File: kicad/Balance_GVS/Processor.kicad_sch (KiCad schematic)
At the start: 21 parts, among them SW3 SW_Push, SW4 SW_Push, U1 ESP32-WROOM-32E, U10 INA219BxD, U2 ESP32-WROOM-32E-N4, U9 MCP4725xxx-xCH

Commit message: Add 3.3V Voltage Regulator and ESP32 Battery ADC
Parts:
- added R33, R34: 10K, symbol Device:R
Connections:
- net GND: now also R34.2
- net Battery_ADC: now reaches U1.8 (IO32)
- net Battery_ADC: now also R33.2, R34.1
- new net Battery_Voltage: R33.1

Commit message: Started adding howland connections
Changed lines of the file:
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@@
 	)
 	(global_label "DAC_OUT"
-		(shape input)
+		(shape output)
 		(at 153.67 63.5 0)
 		(fields_autoplaced yes)

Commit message: Finish Howland
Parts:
- added C22, C23: 4.7µF, symbol Device:C
- added U6: (no value), Package_TO_SOT_SMD:SOT-89-5_Handsoldering, symbol GVS_Library:R1172H331B-T1-FE
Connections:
- net +3.3V: now also C23.2, U6.5 (VOUT)
- net Battery_Voltage: now also C22.1, U6.1 (CE), U6.4 (VIN)
- net GND: now also C22.2, C23.1, U6.2 (GND)

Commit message: Add Processor User IO
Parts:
- removed U2: ESP32-WROOM-32E-N4, ESP32-WROOM_32E_N4_footprints:ESP32­WROOM­32E_EXP, symbol ESP32-WROOM_32E_N4:ESP32-WROOM-32E-N4
- added C24, C25: 0.1uF, RF_Converter:Balun_Johanson_0900PC15J0013, symbol Device:C
- added D5, D6, D7, D8: LED_Small, symbol Device:LED_Small
- added R43, R44, R49, R50: 10K, symbol Device:R
- added R45, R46, R47, R48: 300, symbol Device:R
- added RV1: R_Potentiometer, Package_SO:TSSOP-20_4.4x6.5mm_P0.65mm, symbol Device:R_Potentiometer
- added SW5, SW6: SW_Push, RF_Module:ESP32-WROOM-32E, symbol Switch:SW_Push
- added SW8: SW_DIP_x02, symbol Switch:SW_DIP_x02
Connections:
- net +3.3V: now also R43.1, R44.1, R49.1, R50.1, RV1.1
- net GND: now also C24.2, C25.2, D5.1 (K), D6.1 (K), D7.1 (K), D8.1 (K), RV1.3, SW5.1, SW6.1, SW8.3, SW8.4
- net Button2: now reaches U1.10 (IO25)
- net Button2: now also C25.1, R44.2, SW6.2
- net Switch1: now reaches U1.11 (IO26)
- net Switch1: now also R49.2, SW8.1
- net Switch2: now reaches U1.12 (IO27)
- net Switch2: now also R50.2, SW8.2
- net LED2: now reaches U1.13 (IO14)
- net LED2: now also R46.2
- net LED1: now reaches U1.16 (IO13)
- net LED1: now also R45.2
- net LED3: now reaches U1.23 (IO15)
- net LED3: now also R47.2
- net LED4: now reaches U1.27 (IO16)
- net LED4: now also R48.2
- net Button1: now reaches U1.37 (IO23)
- net Button1: now also C24.1, R43.2, SW5.2
- net POT_ADC: now reaches U1.9 (IO33)
- net POT_ADC: now also RV1.2
- new net: D8.2 (A), R48.1
- new net: D5.2 (A), R45.1
- new net: D7.2 (A), R47.1
- new net: D6.2 (A), R46.1
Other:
- moved on the sheet: C11, C12, C13, C14, C15, C16, C22, C23, R1, R21, R22, R23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

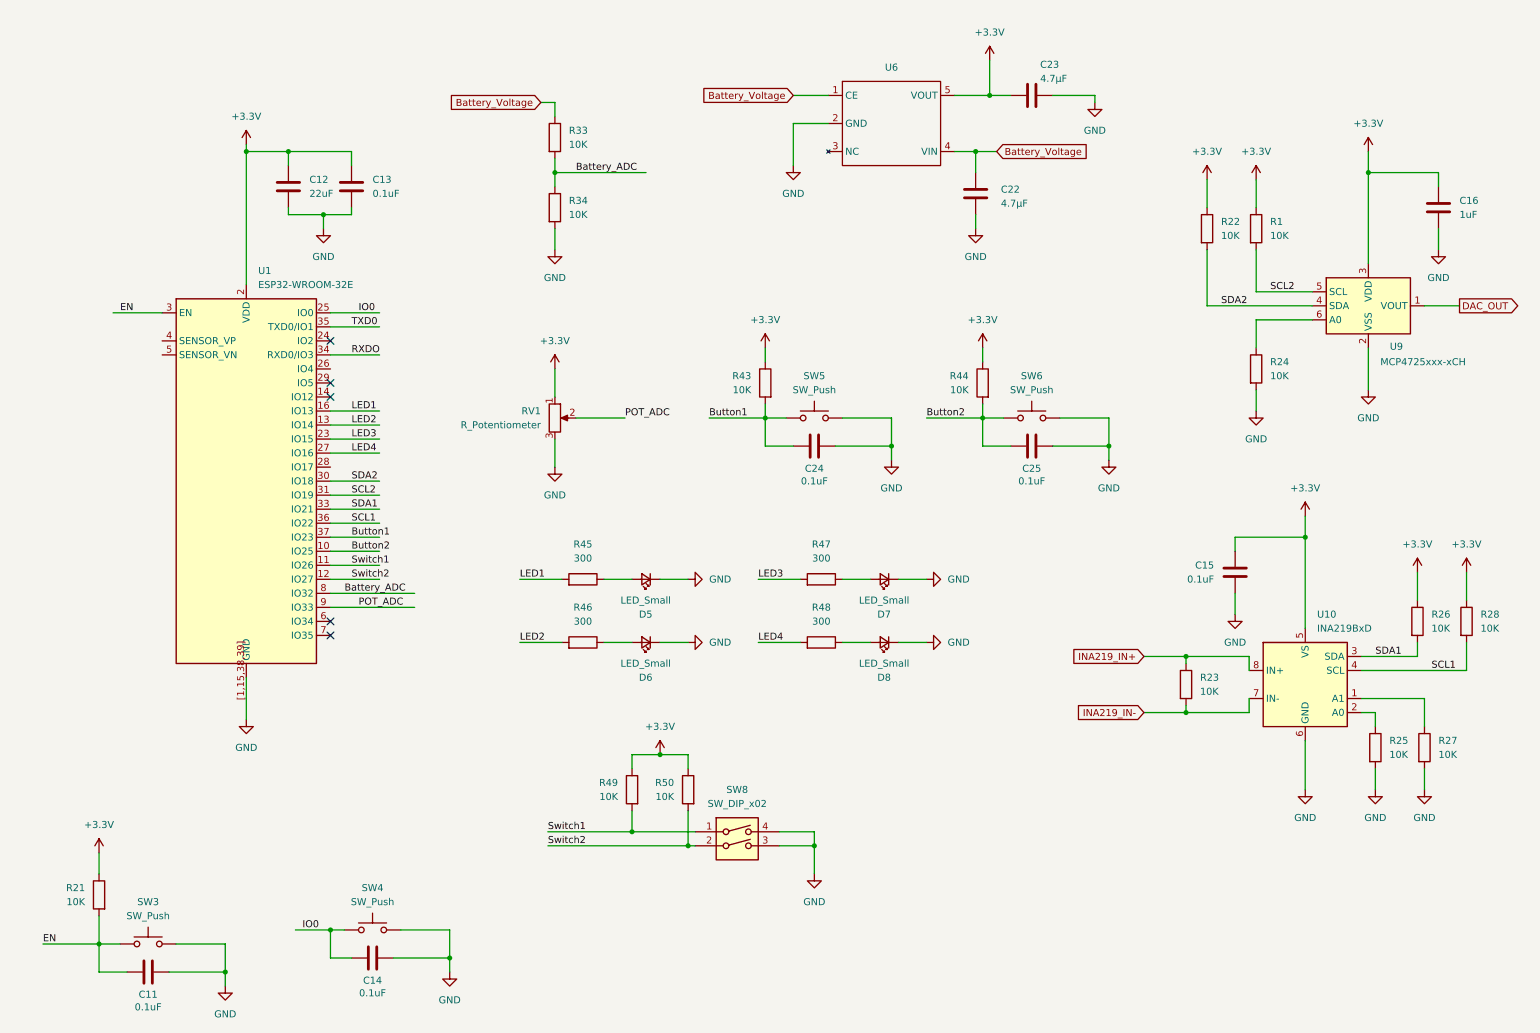
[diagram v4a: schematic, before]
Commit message: Add Footprints to Schematic
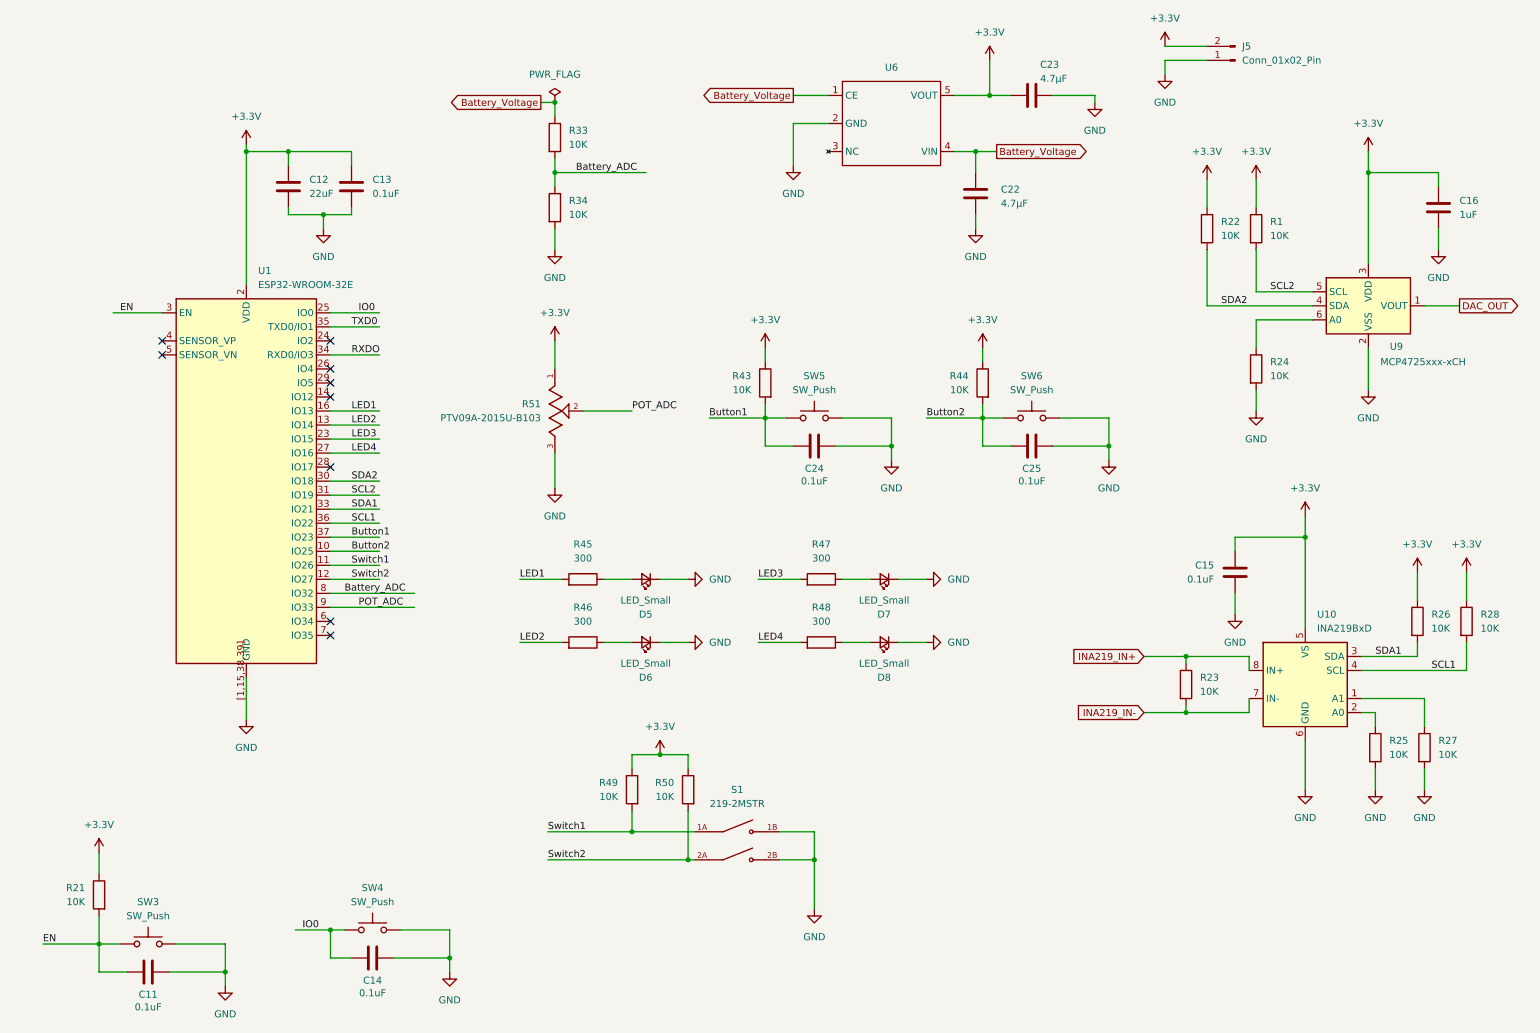
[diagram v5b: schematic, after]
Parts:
- removed RV1: R_Potentiometer, Package_SO:TSSOP-20_4.4x6.5mm_P0.65mm, symbol Device:R_Potentiometer
- removed SW8: SW_DIP_x02, symbol Switch:SW_DIP_x02
- added J5: Conn_01x02_Pin, Connector_PinSocket_2.54mm:PinSocket_1x02_P2.54mm_Vertical, symbol Connector:Conn_01x02_Pin
- added R51: PTV09A-2015U-B103, PTV09A_2015U_B103:TRIM_PTV09A-2015U-B103, symbol PTV09A_2015U_B103:PTV09A-2015U-B103
- added S1: 219-2MSTR, 219_2MSTR:SW_219-2MSTR, symbol 219_2MSTR:219-2MSTR
- C11, C14, C24, C25: footprint RF_Converter:Balun_Johanson_0900PC15J0013 -> Capacitor_SMD:C_0805_2012Metric_Pad1.18x1.45mm_HandSolder
- C12, C13, C15, C16, C22, C23: footprint (none) -> Capacitor_SMD:C_0805_2012Metric_Pad1.18x1.45mm_HandSolder
- D5, D6, D7, D8: footprint (none) -> LED_SMD:LED_0603_1608Metric_Pad1.05x0.95mm_HandSolder
- R1, R21, R22, R23, R24, R25, R26, R27, R28, R33, R34, R43, R44, R45, R46, R47, R48, R49, R50: footprint (none) -> Resistor_SMD:R_0805_2012Metric_Pad1.20x1.40mm_HandSolder
- SW3, SW4, SW5, SW6: footprint RF_Module:ESP32-WROOM-32E -> FSMSMTR:SWITCH_FSMSMTR_TYC
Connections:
- net +3.3V: now also J5.2 (Pin_2), R51.1
- net GND: now also J5.1 (Pin_1), R51.3, S1.1B, S1.2B
- net POT_ADC: now also R51.2
- net Switch1: now also S1.1A
- net Switch2: now also S1.2A
- no-connect marks 5 -> 9

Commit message: Add shit ton to schematic
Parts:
- added J10: I2C Header 2, Connector_PinSocket_2.54mm:PinSocket_1x02_P2.54mm_Vertical, symbol Connector:Conn_01x02_Pin
- added J9: I2C Header 1, Connector_PinSocket_2.54mm:PinSocket_1x02_P2.54mm_Vertical, symbol Connector:Conn_01x02_Pin
- R23: value 10K -> 33
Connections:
- net SCL1: now also J10.2 (Pin_2)
- net SCL2: now also J9.2 (Pin_2)
- net SDA1: now also J10.1 (Pin_1)
- net SDA2: now also J9.1 (Pin_1)
- net INA219_IN+ renamed Safety-
- net INA219_IN- renamed Current_Sense-
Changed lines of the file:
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@@
 	(wire
 		(pts
-			(xy 68.58 106.68) (xy 77.47 106.68)
+			(xy 68.58 106.68) (xy 81.28 106.68)
 		)
 		(stroke
@@
 	(wire
 		(pts
-			(xy 68.58 104.14) (xy 77.47 104.14)
+			(xy 68.58 104.14) (xy 81.28 104.14)
 		)
 		(stroke
@@
 	(wire
 		(pts
-			(xy 68.58 99.06) (xy 77.47 99.06)
+			(xy 68.58 99.06) (xy 81.28 99.06)
 		)
 		(stroke
@@
 	(wire
 		(pts
-			(xy 68.58 101.6) (xy 77.47 101.6)
+			(xy 68.58 101.6) (xy 81.28 101.6)
 		)
 		(stroke
@@
 		)
 	)
-	(global_label "Battery_Voltage"
-		(shape output)
-		(at 152.4 29.21 180)
+	(global_label "Current_Sense-"
+		(shape bidirectional)
+		(at 215.9 140.97 180)
 		(fields_autoplaced yes)
 		(effects
@@
 		)
 		(property "Intersheetrefs" "${INTERSHEET_REFS}"
-			(at 134.7193 29.21 0)
+			(at 196.745 140.97 0)
 			(hide yes)
 			(show_name no)
@@
 		)
 	)
-	(global_label "DAC_OUT"
+	(global_label "Battery_Voltage"
 		(shape output)
-		(at 273.05 67.31 0)
+		(at 152.4 29.21 180)
 		(fields_autoplaced yes)
 		(effects
@@
 				(size 1.27 1.27)
 			)
-			(justify left)
+			(justify right)
 		)
 		(property "Intersheetrefs" "${INTERSHEET_REFS}"
-			(at 284.26 67.31 0)
+			(at 134.7193 29.21 0)
 			(hide yes)
 			(show_name no)
@@
 					(size 1.27 1.27)
 				)
-				(justify left)
+				(justify right)
 			)
 		)
 	)
-	(global_label "Battery_Voltage"
+	(global_label "DAC_OUT"
 		(shape output)
-		(at 106.68 30.48 180)
+		(at 273.05 67.31 0)
 		(fields_autoplaced yes)
 		(effects
@@
 				(size 1.27 1.27)
 			)
-			(justify right)
+			(justify left)
 		)
 		(property "Intersheetrefs" "${INTERSHEET_REFS}"
-			(at 88.9993 30.48 0)
+			(at 284.26 67.31 0)
 			(hide yes)
 			(show_name no)
@@
 					(size 1.27 1.27)
 				)
-				(justify right)
+				(justify left)
 			)
 		)
 	)
-	(global_label "INA219_IN-"
-		(shape input)
-		(at 215.9 140.97 180)
+	(global_label "Battery_Voltage"
+		(shape output)
+		(at 106.68 30.48 180)
 		(fields_autoplaced yes)
 		(effects
@@
 		)
 		(property "Intersheetrefs" "${INTERSHEET_REFS}"
-			(at 201.7871 140.97 0)
+			(at 88.9993 30.48 0)
 			(hide yes)
 			(show_name no)
@@
 		)
 	)
-	(global_label "INA219_IN+"
-		(shape input)
+	(global_label "Safety-"
+		(shape bidirectional)
 		(at 215.9 130.81 180)
 		(fields_autoplaced yes)
@@
 		)
 		(property "Intersheetrefs" "${INTERSHEET_REFS}"
-			(at 201.7871 130.81 0)
+			(at 204.365 130.81 0)
 			(hide yes)
 			(show_name no)
@@
 	)
 	(symbol
+		(lib_id "Connector:Conn_01x02_Pin")
+		(at 86.36 104.14 0)
+		(mirror y)
+		(unit 1)
+		(body_style 1)
+		(exclude_from_sim no)
+		(in_bom yes)
+		(on_board yes)
+		(in_pos_files yes)
+		(dnp no)
+		(property "Reference" "J10"
+			(at 87.63 106.6801 0)
+			(show_name no)
+			(do_not_autoplace no)
+			(effects
+				(font
+					(size 1.27 1.27)
+				)
+				(justify right)
+			)
+		)
+		(property "Value" "I2C Header 2"
+			(at 87.63 104.1401 0)
+			(show_name no)
+			(do_not_autoplace no)
+			(effects
+				(font
+					(size 1.27 1.27)
+				)
+				(justify right)
+			)
+		)
+		(property "Footprint" "Connector_PinSocket_2.54mm:PinSocket_1x02_P2.54mm_Vertical"
+			(at 86.36 104.14 0)
+			(hide yes)
+			(show_name no)
+			(do_not_autoplace no)
+			(effects
+				(font
+					(size 1.27 1.27)
+				)
+			)
+		)
+		(property "Datasheet" ""
+			(at 86.36 104.14 0)
+			(hide yes)
+			(show_name no)
+			(do_not_autoplace no)
+			(effects
+				(font
+					(size 1.27 1.27)
+				)
+			)
+		)
+		(property "Description" "Generic connector, single row, 01x02, script generated"
+			(at 86.36 104.14 0)
+			(hide yes)
+			(show_name no)
+			(do_not_autoplace no)
+			(effects
+				(font
+					(size 1.27 1.27)
+				)
+			)
+		)
+		(pin "1"
+		)
+		(pin "2"
+		)
+		(instances
+			(project "Balance_GVS"
+				(path "/fe65ed2a-e0ad-4542-81bb-0c202b789e4d/1c6ab31e-37ae-4dd6-8c88-946e95d9ae91"
+					(reference "J10")
+					(unit 1)
+				)
+			)
+		)
+	)
+	(symbol
 		(lib_id "power:GND")
 		(at 257.81 154.94 0)
@@
 			)
 		)
-		(property "Value" "10K"
+		(property "Value" "33"
 			(at 226.06 137.1599 0)
 			(show_name no)
@@
 					(unit 1)
 				)
+			)
+		)
+	)
+	(symbol
+		(lib_id "Connector:Conn_01x02_Pin")
+		(at 86.36 99.06 0)
+		(mirror y)
+		(unit 1)
+		(body_style 1)
+		(exclude_from_sim no)
+		(in_bom yes)
+		(on_board yes)
+		(in_pos_files yes)
+		(dnp no)
+		(property "Reference" "J9"
+			(at 87.63 101.6001 0)
+			(show_name no)
+			(do_not_autoplace no)
+			(effects
+				(font
+					(size 1.27 1.27)
+				)
+				(justify right)
+			)
+		)
+		(property "Value" "I2C Header 1"
+			(at 87.63 99.0601 0)
+			(show_name no)
+			(do_not_autoplace no)
+			(effects
+				(font
+					(size 1.27 1.27)
+				)
+				(justify right)
+			)
+		)
+		(property "Footprint" "Connector_PinSocket_2.54mm:PinSocket_1x02_P2.54mm_Vertical"
+			(at 86.36 99.06 0)
+			(hide yes)
+			(show_name no)
+			(do_not_autoplace no)
+			(effects
+				(font
+					(size 1.27 1.27)
+				)
+			)
+		)
+		(property "Datasheet" ""
+			(at 86.36 99.06 0)
+			(hide yes)
+			(show_name no)
+			(do_not_autoplace no)
+			(effects
+				(font
+					(size 1.27 1.27)
+				)
+			)
+		)
+		(property "Description" "Generic connector, single row, 01x02, script generated"
+			(at 86.36 99.06 0)
+			(hide yes)
+			(show_name no)
+			(do_not_autoplace no)
+			(effects
+				(font
+					(size 1.27 1.27)
+				)
+			)
+		)
+		(pin "1"
+		)
+		(pin "2"
+		)
+		(instances
+			(project "Balance_GVS"
+				(path "/fe65ed2a-e0ad-4542-81bb-0c202b789e4d/1c6ab31e-37ae-4dd6-8c88-946e95d9ae91"
+					(reference "J9")
+					(unit 1)
+				)

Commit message: Fixed schematic warnings
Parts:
- removed D5, D6, D7, D8: LED_Small, LED_SMD:LED_0603_1608Metric_Pad1.05x0.95mm_HandSolder, symbol Device:LED_Small
- added D1, D2, D5, D6: LED, LED_SMD:LED_0603_1608Metric_Pad1.05x0.95mm_HandSolder, symbol Device:LED
- added J12: Conn_01x02_Pin, Connector_PinSocket_2.54mm:PinSocket_1x02_P2.54mm_Vertical, symbol Connector:Conn_01x02_Pin
- added J13: UART Header, Connector_PinSocket_2.54mm:PinSocket_1x02_P2.54mm_Vertical, symbol Connector:Conn_01x02_Pin
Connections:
- net Battery_Voltage: now also J12.2 (Pin_2)
- net GND: now also D1.1 (K), D2.1 (K), D5.1 (K), D6.1 (K), J12.1 (Pin_1)
- net RXDO: now also J13.1 (Pin_1)
- net TXD0: now also J13.2 (Pin_2)
- net at R48.1: now also D6.2 (A)
- net at R45.1: now also D1.2 (A)
- net at R47.1: now also D5.2 (A)
- net at R46.1: now also D2.2 (A)

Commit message: I kinda popped off ngl. Main pcb almost done
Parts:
- added J15, J4: Conn_01x01_Pin, Connector_PinSocket_2.54mm:PinSocket_1x01_P2.54mm_Vertical, symbol Connector:Conn_01x01_Pin
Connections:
- net EN: now also J15.1 (Pin_1)
- net IO0: now also J4.1 (Pin_1)
- net Switch1: now also R50.2, S1.2A; no longer R49.2, S1.1A
- net Switch2: now also R49.2, S1.1A; no longer R50.2, S1.2A
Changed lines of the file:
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@@
 	)
 	(junction
+		(at 71.12 185.42)
+		(diameter 0)
+		(color 0 0 0 0)
+	)
+	(junction
 		(at 156.21 167.64)
 		(diameter 0)
@@
 	)
 	(junction
+		(at 26.67 187.96)
+		(diameter 0)
+		(color 0 0 0 0)
+	)
+	(junction
 		(at 68.58 180.34)
 		(diameter 0)
@@
 	(wire
 		(pts
+			(xy 71.12 190.5) (xy 71.12 185.42)
+		)
+		(stroke
+			(width 0)
+			(type default)
+		)
+	)
+	(wire
+		(pts
 			(xy 181.61 29.21) (xy 187.96 29.21)
 		)
@@
 	(wire
 		(pts
+			(xy 24.13 194.31) (xy 26.67 194.31)
+		)
+		(stroke
+			(width 0)
+			(type default)
+		)
+	)
+	(wire
+		(pts
 			(xy 128.27 148.59) (xy 133.35 148.59)
 		)
@@
 	(wire
 		(pts
+			(xy 71.12 185.42) (xy 68.58 185.42)
+		)
+		(stroke
+			(width 0)
+			(type default)
+		)
+	)
+	(wire
+		(pts
 			(xy 245.11 146.05) (xy 245.11 154.94)
 		)
@@
 	(wire
 		(pts
+			(xy 26.67 194.31) (xy 26.67 187.96)
+		)
+		(stroke
+			(width 0)
+			(type default)
+		)
+	)
+	(wire
+		(pts
 			(xy 246.38 69.85) (xy 236.22 69.85)
 		)
@@
 	(wire
 		(pts
-			(xy 72.39 185.42) (xy 68.58 185.42)
+			(xy 72.39 185.42) (xy 71.12 185.42)
 		)
 		(stroke
@@
 	(wire
 		(pts
+			(xy 68.58 190.5) (xy 71.12 190.5)
+		)
+		(stroke
+			(width 0)
+			(type default)
+		)
+	)
+	(wire
+		(pts
 			(xy 31.75 187.96) (xy 26.67 187.96)
 		)
@@
 		)
 	)
-	(label "Switch1"
+	(label "Switch2"
 		(at 107.95 162.56 0)
 		(effects
@@
 		)
 	)
-	(label "Switch2"
+	(label "Switch1"
 		(at 107.95 167.64 0)
 		(effects
@@
 	)
 	(symbol
+		(lib_id "Connector:Conn_01x01_Pin")
+		(at 19.05 194.31 0)
+		(unit 1)
+		(body_style 1)
+		(exclude_from_sim no)
+		(in_bom yes)
+		(on_board yes)
+		(in_pos_files yes)
+		(dnp no)
+		(fields_autoplaced yes)
+		(property "Reference" "J15"
+			(at 19.685 189.23 0)
+			(show_name no)
+			(do_not_autoplace no)
+			(effects
+				(font
+					(size 1.27 1.27)
+				)
+			)
+		)
+		(property "Value" "Conn_01x01_Pin"
+			(at 19.685 191.77 0)
+			(show_name no)
+			(do_not_autoplace no)
+			(effects
+				(font
+					(size 1.27 1.27)
+				)
+			)
+		)
+		(property "Footprint" "Connector_PinSocket_2.54mm:PinSocket_1x01_P2.54mm_Vertical"
+			(at 19.05 194.31 0)
+			(hide yes)
+			(show_name no)
+			(do_not_autoplace no)
+			(effects
+				(font
+					(size 1.27 1.27)
+				)
+			)
+		)
+		(property "Datasheet" ""
+			(at 19.05 194.31 0)
+			(hide yes)
+			(show_name no)
+			(do_not_autoplace no)
+			(effects
+				(font
+					(size 1.27 1.27)
+				)
+			)
+		)
+		(property "Description" "Generic connector, single row, 01x01, script generated"
+			(at 19.05 194.31 0)
+			(hide yes)
+			(show_name no)
+			(do_not_autoplace no)
+			(effects
+				(font
+					(size 1.27 1.27)
+				)
+			)
+		)
+		(pin "1"
+		)
+		(instances
+			(project "Balance_GVS"
+				(path "/fe65ed2a-e0ad-4542-81bb-0c202b789e4d/1c6ab31e-37ae-4dd6-8c88-946e95d9ae91"
+					(reference "J15")
+					(unit 1)
+				)
+			)
+		)
+	)
+	(symbol
 		(lib_id "Device:C")
 		(at 156.21 92.71 90)
@@
 					(unit 1)
 				)
+			)
+		)
+	)
+	(symbol
+		(lib_id "Connector:Conn_01x01_Pin")
+		(at 63.5 190.5 0)
+		(unit 1)
+		(body_style 1)
+		(exclude_from_sim no)
+		(in_bom yes)
+		(on_board yes)
+		(in_pos_files yes)
+		(dnp no)
+		(fields_autoplaced yes)
+		(property "Reference" "J4"
+			(at 64.135 185.42 0)
+			(show_name no)
+			(do_not_autoplace no)
+			(effects
+				(font
+					(size 1.27 1.27)
+				)
+			)
+		)
+		(property "Value" "Conn_01x01_Pin"
+			(at 64.135 187.96 0)
+			(show_name no)
+			(do_not_autoplace no)
+			(effects
+				(font
+					(size 1.27 1.27)
+				)
+			)
+		)
+		(property "Footprint" "Connector_PinSocket_2.54mm:PinSocket_1x01_P2.54mm_Vertical"
+			(at 63.5 190.5 0)
+			(hide yes)
+			(show_name no)
+			(do_not_autoplace no)
+			(effects
+				(font
+					(size 1.27 1.27)
+				)
+			)
+		)
+		(property "Datasheet" ""
+			(at 63.5 190.5 0)
+			(hide yes)
+			(show_name no)
+			(do_not_autoplace no)
+			(effects
+				(font
+					(size 1.27 1.27)
+				)
+			)
+		)
+		(property "Description" "Generic connector, single row, 01x01, script generated"
+			(at 63.5 190.5 0)
+			(hide yes)
+			(show_name no)
+			(do_not_autoplace no)
+			(effects
+				(font
+					(size 1.27 1.27)
+				)
+			)
+		)
+		(pin "1"
+		)
+		(instances
+			(project "Balance_GVS"
+				(path "/fe65ed2a-e0ad-4542-81bb-0c202b789e4d/1c6ab31e-37ae-4dd6-8c88-946e95d9ae91"
+					(reference "J4")
+					(unit 1)
+				)
